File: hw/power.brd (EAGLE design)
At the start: 68 x 27 mm, 18 parts, among them U1 TPS54200, U7 MIC5233

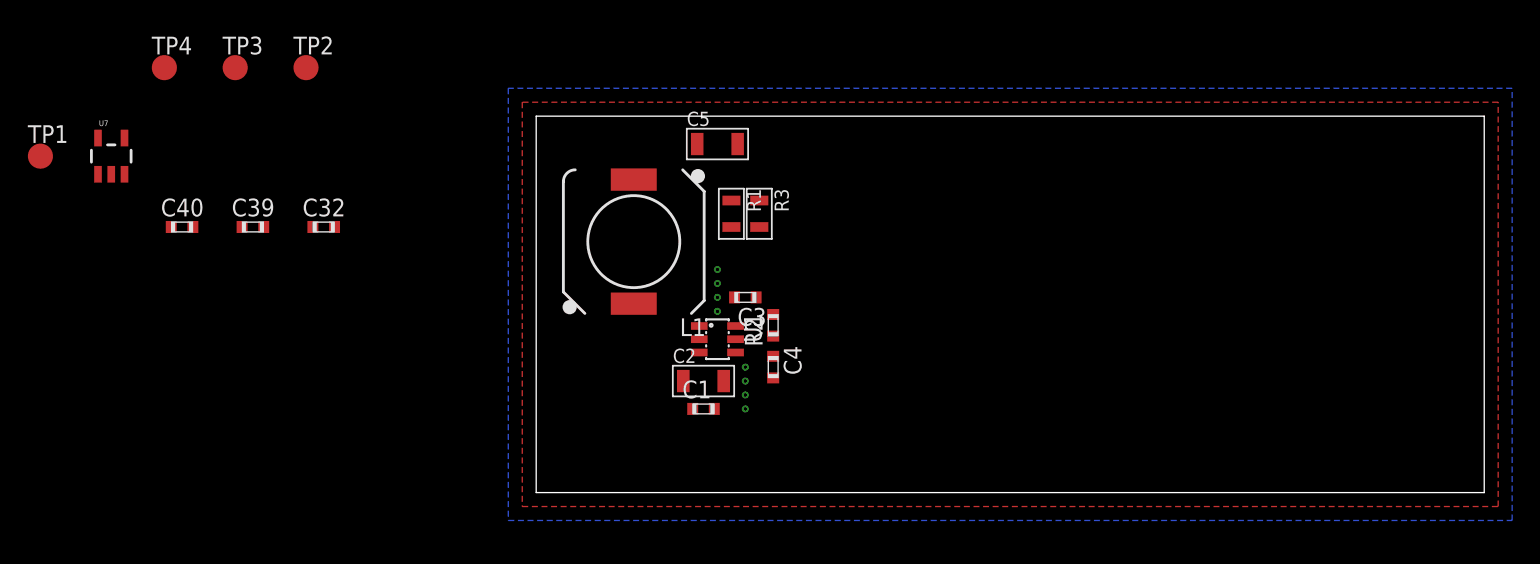
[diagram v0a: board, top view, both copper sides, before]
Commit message: power: power routed, control placed
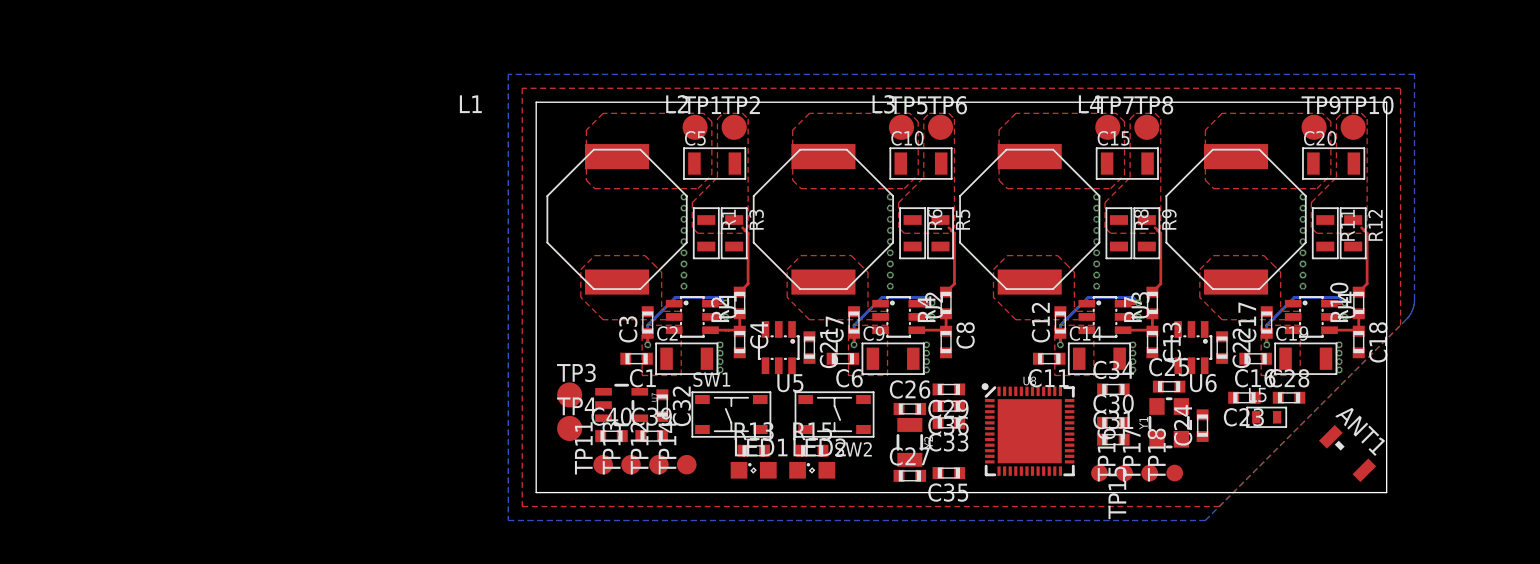
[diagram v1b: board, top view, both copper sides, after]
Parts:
- added ANT1: WE-MCA-7488930245, balto:WE-MCA
- added C10, C14, C15, C19, C20, C9: 10u, MF_Passives:C1206
- added C11, C12, C16, C17, C33, C34, C35, C36, C6, C7: .1u, balto:0603
- added C13, C18, C8: 82n, balto:0603
- added C21, C22: (no value), balto:0603
- added C23: .8p, balto:0603
- added C24, C25: 33p, balto:0603
- added C26, C27: 16p, balto:0603
- added C28, C31: dnp, balto:0603
- added C29: 1u, balto:0603
- added C30: 100p, balto:0603
- added L2, L3, L4: WE-TPC, balto:WE-TPC_INDUCTOR
- added L5: 3n9, MF_Passives:L0603
- added LED1, LED2: (no value), led:SML0805
- added R10, R4, R7: 910, balto:0603
- added R11, R12, R5, R6, R8, R9: tbd, MF_Passives:R0805
- added R13, R15: 1k, balto:0603
- added SW1, SW2: MF-SW-TACT-4.2MM, MF_Switches:TACT4.2MM
- added TP10, TP5, TP6, TP7, TP8, TP9: TPTP18R, testpad:TP18R
- added TP11, TP12, TP13, TP14: TPTP14R, testpad:TP14R
- added TP15, TP16, TP17, TP18: TPTP12R, testpad:TP12R
- added U2, U3, U4: TPS54200, balto:SOT23-6L
- added U5, U6: MIC280, balto:SOT23-6L
- added U8: NRF52832, SparkFun-RF:QFN48-6X6MM
- added Y1: 32MHz, SparkFun-Clocks:CRYSTAL-SMD-3.2X2.5MM
- added Y2: 32.768kHz, SparkFun-Clocks:CRYSTAL-SMD-3.2X1.5MM
- L1: value DR1030 -> WE-TPC; device inductors:DR1030 -> balto:WE-TPC_INDUCTOR
- moved TP1 47.0 mm to (11.4, 26.2)
- moved U7 40.7 mm to (6.13, 6.28), turned to 270 degrees
- moved TP4 38.9 mm to (2.40, 4.60)
- moved C40 34.3 mm to (5.40, 4.05)
- moved TP3 33.6 mm to (2.40, 7.00)
- moved C39 32.3 mm to (8.28, 4.05)
- moved TP2 31.0 mm to (14.2, 26.2)
- moved C32 27.5 mm to (9.05, 6.24), turned to 270 degrees
- moved C3 7.23 mm to (8.00, 12.2), turned to 90 degrees
- moved C1 6.00 mm to (7.20, 9.60), turned to 180 degrees
- moved C4 3.00 mm to (14.6, 10.8)
- moved R2 2.88 mm to (14.6, 13.6)
- moved U1 2.41 mm to (11.2, 12.6)
- moved R1 2.28 mm to (12.2, 18.6)
- moved R3 2.28 mm to (14.2, 18.6)
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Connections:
- net PWM renamed PWM1
- new net ANT: C23.1, L5.P$1, U8.30
- new net LED1: R15.2
- new net LED2: R13.2
- new net N$10: C10.P$1, L2.P$2, TP5.TP
- new net N$11: C12.2, L3.P$1, U3.2
- new net N$12: C12.1, U3.6
- new net N$13: C13.1, R7.1, U3.4
- new net N$14: C15.P$2, R7.2, R8.P$1, R9.P$1, TP8.TP
- new net N$15: C15.P$1, L3.P$2, TP7.TP
- new net N$16: C17.2, L4.P$1, U4.2
- new net N$17: C17.1, U4.6
- new net N$18: C18.1, R10.1, U4.4
- new net N$19: C20.P$2, R10.2, R11.P$1, R12.P$1, TP10.TP
- new net N$20: C20.P$1, L4.P$2, TP9.TP
- new net N$21: LED1.C, R13.1
- new net N$22: ANT1.FEED, C28.1, L5.P$2
- new net N$23: LED2.C, R15.1
- new net N$24: C29.1, U8.46
- new net N$25: C30.1, U8.33
- new net N$26: C31.1, U8.32
- new net N$27: C33.1, U8.1
- new net N$6: C7.2, L2.P$1, U2.2
- new net N$7: C7.1, U2.6
- new net N$8: C8.1, R4.1, U2.4
- new net N$9: C10.P$2, R4.2, R5.P$1, R6.P$1, TP6.TP
- new net PWM2: U2.5
- new net PWM3: U3.5
- new net PWM4: U4.5
- new net SCL: TP12.TP, U5.4, U6.4
- new net SDA: TP13.TP, U5.5, U6.5
- new net SW1: SW1.P$2
- new net SW2: SW2.P$2
- new net SWDCLK: TP17.TP, U8.25
- new net SWDIO: TP16.TP, U8.26
- new net XC1: C24.1, U8.34, Y1.1
- new net XC2: C25.1, U8.35, Y1.3
- new net XL1: C26.1, U8.2, Y2.P$1
- new net XL2: C27.1, U8.3, Y2.P$2
- net +3V3: now also C21.1, C22.1, C34.1, C35.1, C36.1, LED1.A, LED2.A, TP11.TP, TP15.TP, U5.1, U6.1, U8.13, U8.36, U8.48
- net GND: now also C11.2, C13.2, C14.P$2, C16.2, C18.2, C19.P$2, C21.2, C22.2, C23.2, C24.2, C25.2, C26.2, C27.2, C28.2, C29.2, C30.2, C31.2, C33.2, C34.2, C35.2, C36.2, C6.2, C8.2, C9.P$2, R11.P$2, R12.P$2, R5.P$2, R6.P$2, R8.P$2, R9.P$2, SW1.P$3, SW1.P$4, SW2.P$3, SW2.P$4, TP14.TP, TP18.TP, U2.1, U3.1, U4.1, U5.2, U6.2, U8.31, U8.45, U8.EP
- net N$1: now also L1.P$1; no longer L1.1
- net N$3: now also L1.P$2; no longer L1.2
- net VCC: now also C11.1, C14.P$1, C16.1, C19.P$1, C6.1, C9.P$1, U2.3, U3.3, U4.3
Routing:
- net N$17: track 0.00 -> 9.94 mm, vias 0 -> 2
- net N$2: track 0.00 -> 9.94 mm, vias 0 -> 2
- net N$12: track 0.00 -> 9.94 mm, vias 0 -> 2
- net N$7: track 0.00 -> 9.94 mm, vias 0 -> 2
- net N$9: track 0.00 -> 5.04 mm
- net N$19: track 0.00 -> 5.04 mm
- net N$5: track 0.00 -> 5.04 mm
- net N$14: track 0.00 -> 5.04 mm
- net N$13: track 0.00 -> 3.37 mm
- net N$4: track 0.00 -> 3.37 mm
- net N$18: track 0.00 -> 3.37 mm
- net N$8: track 0.00 -> 3.37 mm
- net PWM4: track 0.00 -> 1.10 mm, vias 0 -> 1
- net PWM3: track 0.00 -> 1.10 mm, vias 0 -> 1
- net PWM1: track 0.00 -> 1.10 mm, vias 0 -> 1
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- added copper zone on layer 1, net N$1
- added copper zone on layer 1, net N$10
- added copper zone on layer 1, net N$11
- added copper zone on layer 1, net N$14
- added copper zone on layer 1, net N$15
- added copper zone on layer 1, net N$16
- added copper zone on layer 1, net N$19
- added copper zone on layer 1, net N$20
- added copper zone on layer 1, net N$3
- added copper zone on layer 1, net N$5
- added copper zone on layer 1, net N$6
- added copper zone on layer 1, net N$9
- added copper zone on layer 1, net VCC
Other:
- board size 68 x 27 mm -> 61 x 28 mm

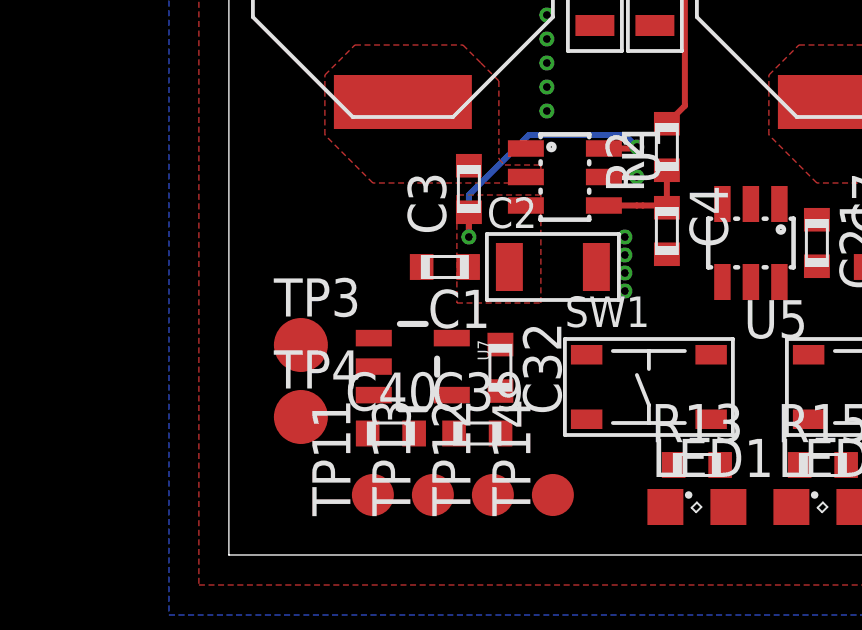
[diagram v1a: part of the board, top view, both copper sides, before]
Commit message: power: add inner layers
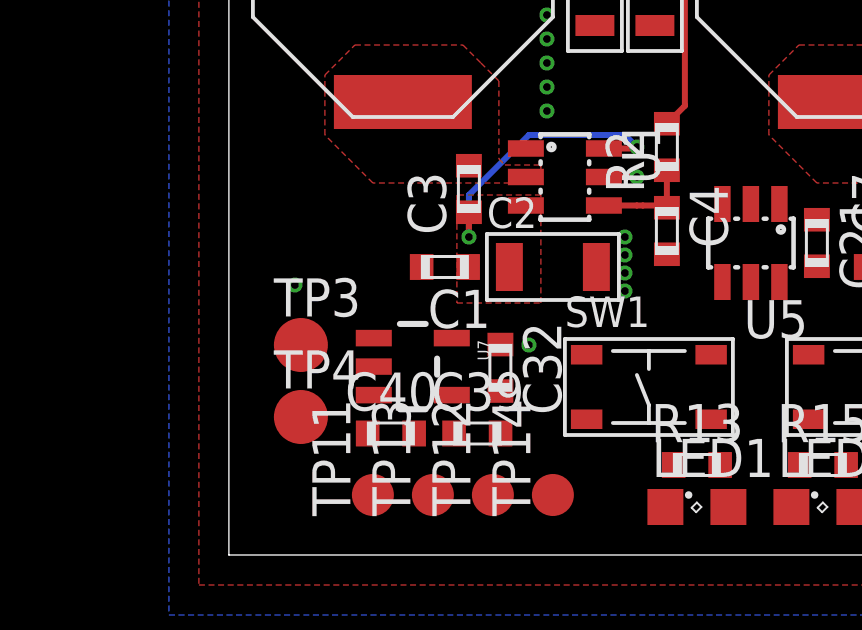
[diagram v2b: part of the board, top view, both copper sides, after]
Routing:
- added copper zone on layer 2, net +3V3
- added copper zone on layer 15, net GND
- added copper zone on layer 2, net GND
- added copper zone on layer 2, net VCC
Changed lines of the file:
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@@
 <setting verticaltext="up"/>
 </settings>
-<grid distance="1" unitdist="mm" unit="mm" style="dots" multiple="1" display="yes" altdistance="5" altunitdist="mil" altunit="mil"/>
+<grid distance="0.2" unitdist="mm" unit="mm" style="dots" multiple="1" display="yes" altdistance="5" altunitdist="mil" altunit="mil"/>
 <layers>
 <layer number="1" name="Top" color="4" fill="1" visible="yes" active="yes"/>
+<layer number="2" name="Route2" color="5" fill="1" visible="yes" active="yes"/>
+<layer number="15" name="Route15" color="2" fill="1" visible="yes" active="yes"/>
 <layer number="16" name="Bottom" color="1" fill="1" visible="yes" active="yes"/>
 <layer number="17" name="Pads" color="2" fill="1" visible="yes" active="yes"/>
@@
 &lt;p&gt;2 Layers: 6 mil clearence, width, annular, 10 mil drill
 &lt;p&gt;4 Layers: 5 mil clearence, width, 10 mil drill, 4 mil annular</description>
-<param name="layerSetup" value="(1*16)"/>
+<param name="layerSetup" value="(1*2+15*16)"/>
 <param name="mtCopper" value="0.035mm 0.035mm 0.035mm 0.035mm 0.035mm 0.035mm 0.035mm 0.035mm 0.035mm 0.035mm 0.035mm 0.035mm 0.035mm 0.035mm 0.035mm 0.035mm"/>
 <param name="mtIsolate" value="1.5mm 0.15mm 0.2mm 0.15mm 0.2mm 0.15mm 0.2mm 0.15mm 0.2mm 0.15mm 0.2mm 0.15mm 0.2mm 0.15mm 0.2mm"/>
@@
 <contactref element="SW2" pad="P$4"/>
 <contactref element="SW2" pad="P$3"/>
+<polygon width="0.1524" layer="2">
+<vertex x="-3" y="12.6"/>
+<vertex x="63.8" y="12.6"/>
+<vertex x="63.8" y="30.8"/>
+<vertex x="-3" y="30.8"/>
+</polygon>
+<polygon width="0.1524" layer="15">
+<vertex x="-4" y="-4"/>
+<vertex x="46" y="-4"/>
+<vertex x="64.8" y="14.8"/>
+<vertex x="64.8" y="31.8"/>
+<vertex x="-4" y="31.8"/>
+</polygon>
 </signal>
 <signal name="+3V3">
@@
 <contactref element="LED2" pad="A"/>
 <contactref element="LED1" pad="A"/>
+<polygon width="0.1524" layer="2">
+<vertex x="-3" y="-3"/>
+<vertex x="49" y="-3"/>
+<vertex x="49" y="7.8"/>
+<vertex x="-3" y="7.8"/>
+</polygon>
+<via x="10" y="7" extent="1-16" drill="0.254"/>
 <wire x1="47.95" y1="11.7" x2="49.2" y2="11.1745" width="0" layer="19" extent="1-1"/>
 <wire x1="40.6255" y1="7.4" x2="47.95" y2="11.7" width="0" layer="19" extent="1-1"/>
@@
 <wire x1="20.85" y1="1.6" x2="30.3745" y2="1.4" width="0" layer="19" extent="1-1"/>
 <wire x1="16.65" y1="1.6" x2="20.85" y2="1.6" width="0" layer="19" extent="1-1"/>
-<wire x1="9.05" y1="7.0145" x2="16.65" y2="1.6" width="0" layer="19" extent="1-1"/>
+<wire x1="10" y1="7" x2="16.65" y2="1.6" width="0" layer="19" extent="1-1"/>
+<wire x1="9.05" y1="7.0145" x2="10" y2="7" width="0" layer="19" extent="1-1"/>
 <wire x1="7.4301" y1="7.23" x2="9.05" y2="7.0145" width="0" layer="19" extent="1-1"/>
 <wire x1="4.8" y1="2" x2="7.4301" y2="7.23" width="0" layer="19" extent="1-1"/>
-<wire x1="19.6" y1="11.1745" x2="20.85" y2="1.6" width="0" layer="19" extent="1-1"/>
-<wire x1="18.35" y1="11.7" x2="19.6" y2="11.1745" width="0" layer="19" extent="1-1"/>
+<wire x1="18.35" y1="11.7" x2="10" y2="7" width="0" layer="19" extent="1-1"/>
+<wire x1="19.6" y1="11.1745" x2="18.35" y2="11.7" width="0" layer="19" extent="1-1"/>
 </signal>
 <signal name="VCC">
@@
 <vertex x="54.8" y="8.4"/>
 </polygon>
+<polygon width="0.1524" layer="2">
+<vertex x="-3" y="8.2"/>
+<vertex x="55.2" y="8.2"/>
+<vertex x="55.2" y="12.2"/>
+<vertex x="-3" y="12.2"/>
+</polygon>
+<via x="2.2" y="9" extent="1-16" drill="0.254"/>
 <wire x1="4.8299" y1="5.33" x2="4.8299" y2="7.23" width="0" layer="19" extent="1-1"/>
 <wire x1="4.6255" y1="4.05" x2="4.8299" y2="5.33" width="0" layer="19" extent="1-1"/>
 <wire x1="2.4" y1="7" x2="4.8299" y2="7.23" width="0" layer="19" extent="1-1"/>
+<wire x1="2.2" y1="9" x2="2.4" y2="7" width="0" layer="19" extent="1-1"/>
 <wire x1="7.9745" y1="9.6" x2="4.8299" y2="7.23" width="0" layer="19" extent="1-1"/>
 <wire x1="22.7745" y1="9.6" x2="9.9" y2="11.65" width="0" layer="19" extent="1-1"/>

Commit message: power: r0?
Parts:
- added R14, R16: 5k6, balto:0603
- added U$1: (no value), cat:CAT-L
- moved TP12 3.42 mm to (5.40, 1.60)
- moved C40 2.98 mm to (5.80, 7.00)
- moved C25 1.61 mm to (44.0, 6.80), turned to 90 degrees
- moved U7 1.52 mm to (5.80, 4.80)
- moved TP14 1.46 mm to (9.40, 1.60)
- moved TP11 1.46 mm to (3.40, 1.60)
- moved C39 1.12 mm to (9.40, 4.00)
- moved Y1 1.08 mm to (46.4, 5.40)
- moved C24 1.00 mm to (48.6, 5.40)
- moved TP18 0.82 mm to (46.6, 1.20)
- moved TP13 0.72 mm to (7.40, 1.60)
- moved TP17 0.63 mm to (44.6, 1.20)
- moved C32 0.45 mm to (8.60, 6.20), turned to 90 degrees
- moved C26 0.45 mm to (26.6, 6.40), turned to 180 degrees
- moved TP16 0.45 mm to (42.6, 1.20)
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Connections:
- net +3V3: now also R14.1, R16.1
- net LED1: now also U8.9
- net LED2: now also U8.10
- net PWM1: now also U8.43
- net PWM2: now also U8.42
- net PWM3: now also U8.41
- net PWM4: now also U8.40
- net SCL: now also R14.2, U8.39
- net SDA: now also R16.2, U8.38
- net SW1: now also U8.7
- net SW2: now also U8.8
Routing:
- net SCL: track 0.00 -> 48.3 mm, vias 0 -> 5
- net SDA: track 0.00 -> 48.1 mm, vias 0 -> 5
- net +3V3: track 0.00 -> 31.6 mm, vias 1 -> 10
- net PWM1: track 1.10 -> 26.9 mm, vias 1 -> 2
- net PWM4: track 1.10 -> 26.9 mm, vias 1 -> 2
- net SW1: track 0.00 -> 18.2 mm, vias 0 -> 2
- net LED2: track 0.00 -> 17.2 mm, vias 0 -> 2
- net ANT: track 0.00 -> 16.4 mm
- net LED1: track 0.00 -> 12.6 mm, vias 0 -> 2
- net XC1: track 0.00 -> 11.5 mm
- net PWM3: track 1.10 -> 12.5 mm, vias 1 -> 2
- net SW2: track 0.00 -> 11.3 mm, vias 0 -> 2
- net PWM2: track 1.10 -> 11.1 mm, vias 1 -> 2
- net XL2: track 0.00 -> 8.66 mm
- net XL1: track 0.00 -> 8.43 mm
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- added copper zone on layer 15, net +3V3
- added copper zone on layer 15, net VCC
- removed copper zone on layer 2, net +3V3
- removed copper zone on layer 2, net VCC
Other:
- outline, holes or cut-outs redrawn
- board text added: "FB2019"
- board text added: "spotlight-power"

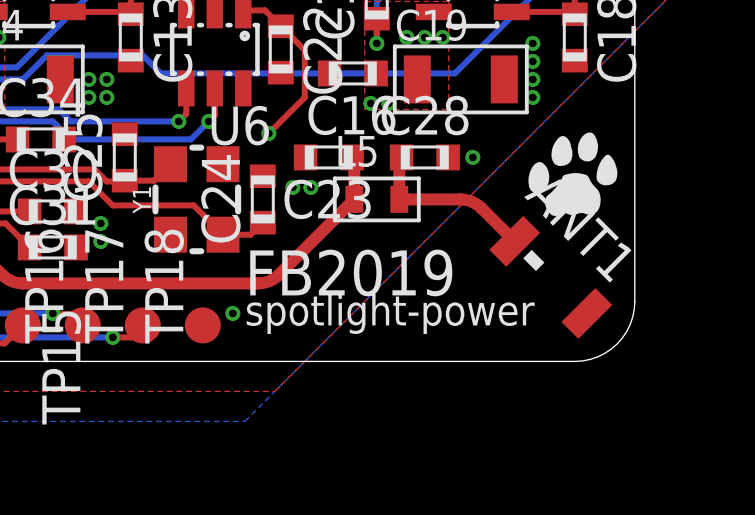
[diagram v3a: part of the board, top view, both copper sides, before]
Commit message: power: schematic refactoring?
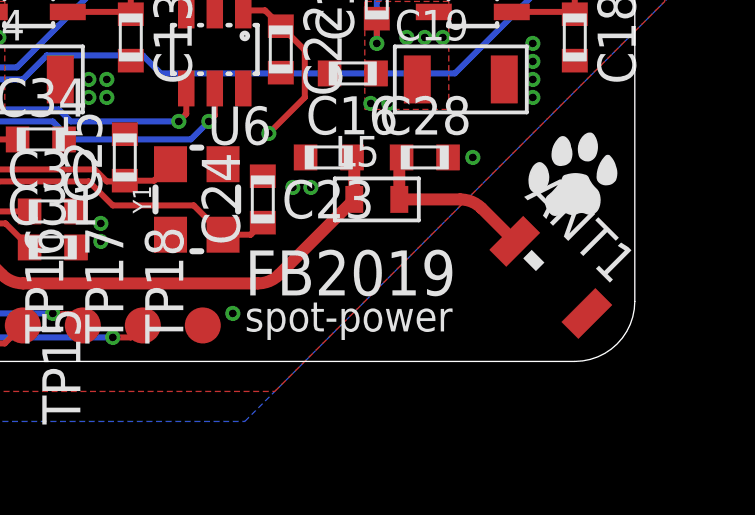
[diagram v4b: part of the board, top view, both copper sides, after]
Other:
- board text added: "spot-power"
- board text removed: "spotlight-power"
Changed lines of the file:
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@@
 <dimension x1="0" y1="28" x2="0" y2="0" x3="-10" y3="14" textsize="1.778" layer="47"/>
 <text x="48" y="2.2" size="1.5" layer="121">FB2019</text>
-<text x="48" y="1.2" size="1" layer="121">spotlight-power</text>
+<text x="48" y="1" size="1" layer="121">spot-power</text>
 </plain>
 <attributes>

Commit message: power: few assembly notes
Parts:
- R13, R15: value 1k -> 680
